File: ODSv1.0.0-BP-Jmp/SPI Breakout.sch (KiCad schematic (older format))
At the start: 3 parts, among them J12 Conn_02x10_Odd_Even, J13 Conn_02x10_Odd_Even, J14 Conn_02x10_Odd_Even

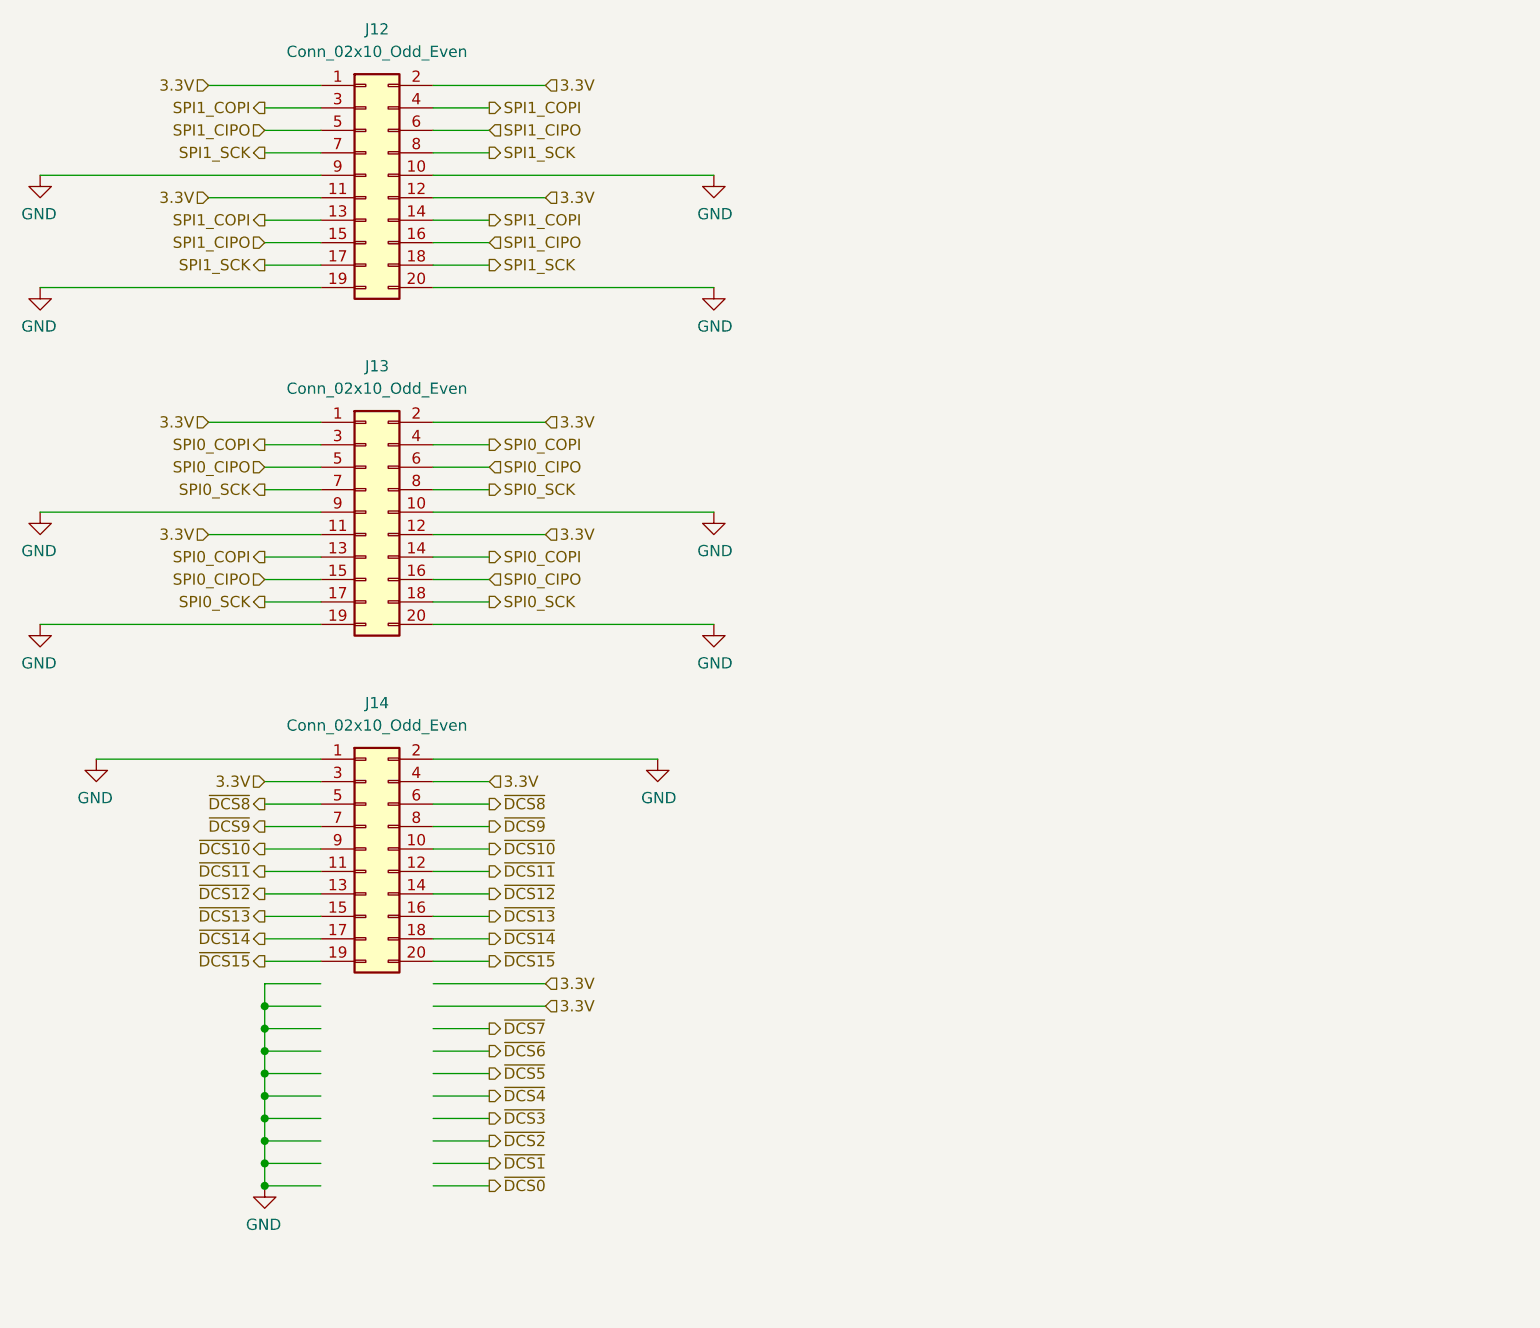
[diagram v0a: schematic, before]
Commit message: Fix hierarchical pin label directions, finish front right corner
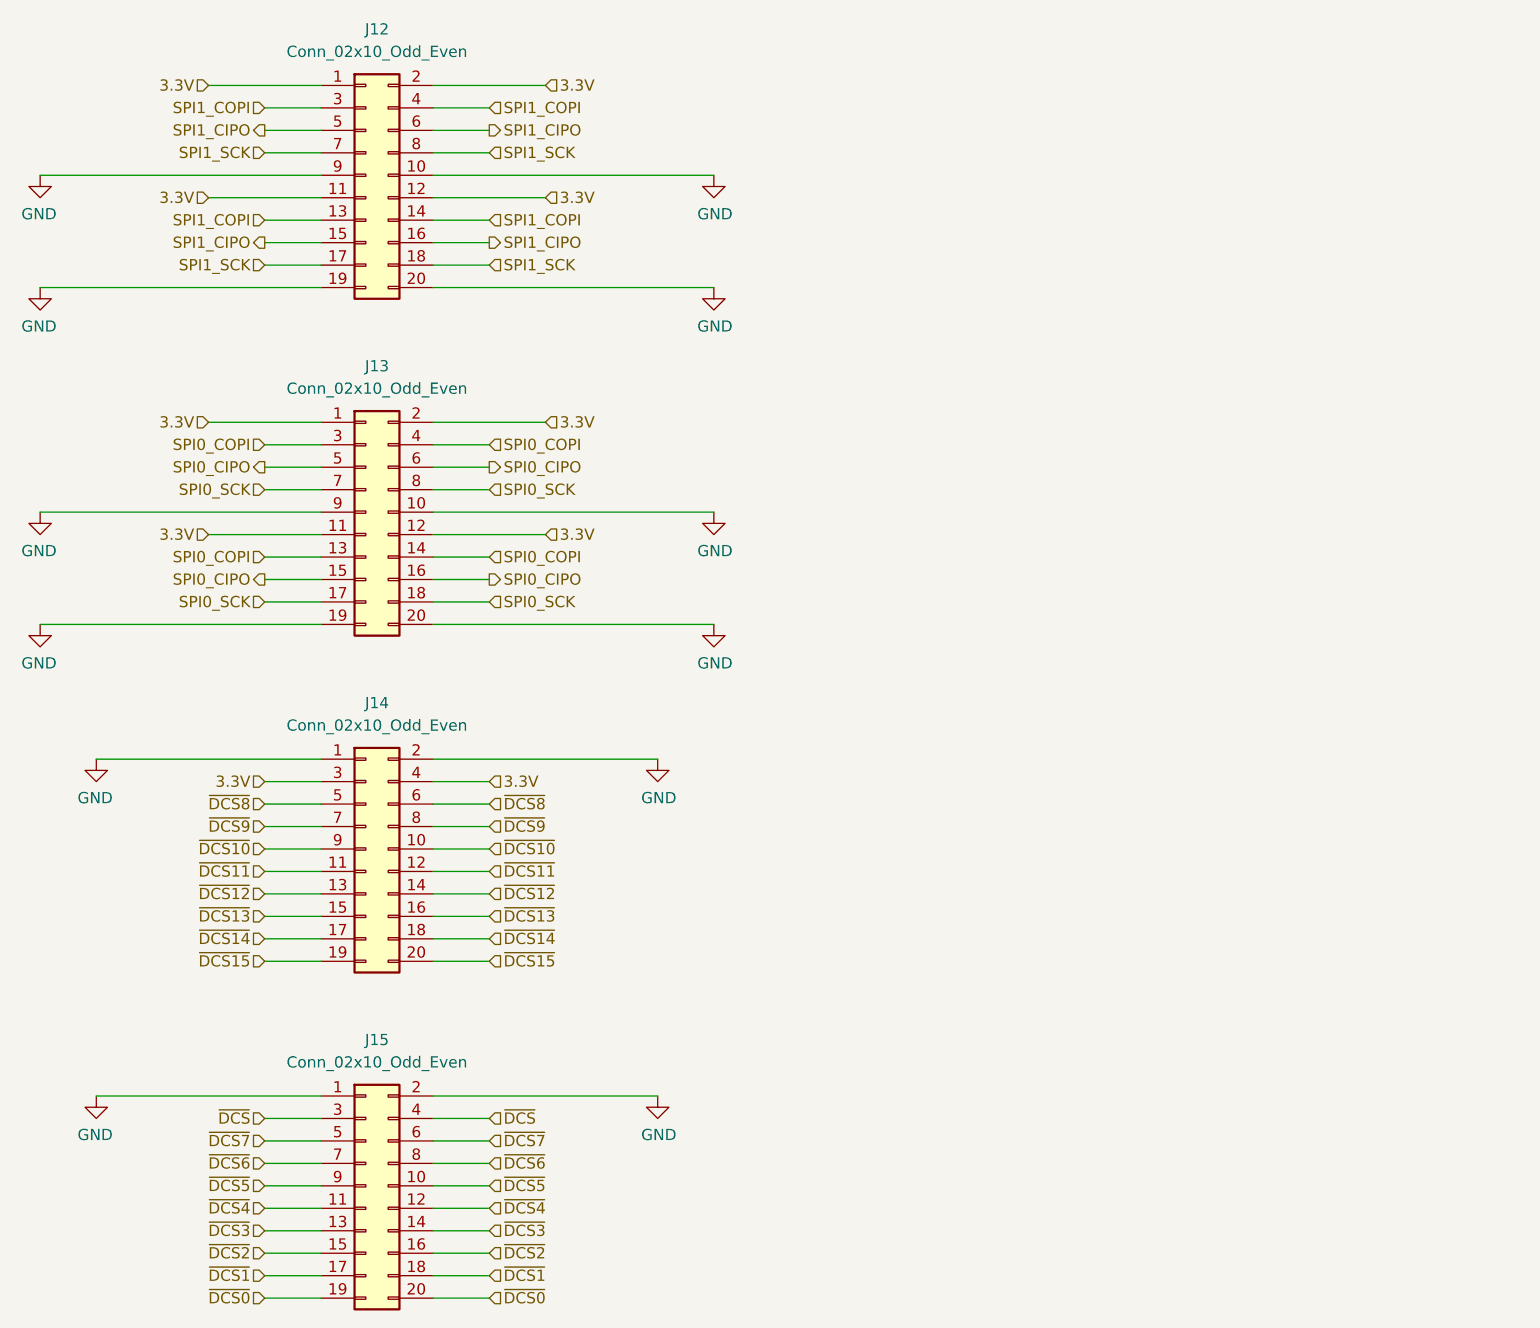
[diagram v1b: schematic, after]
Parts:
- added J15: Conn_02x10_Odd_Even, Connector_PinHeader_2.54mm:PinHeader_2x10_P2.54mm_Vertical_SMD, symbol Connector_Generic:Conn_02x10_Odd_Even
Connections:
- net labels added: ~DCS~
- wire segments 89 -> 80

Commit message: Add a DAC
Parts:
- added J18, J19: Conn_02x10_Odd_Even, Connector_PinHeader_2.54mm:PinHeader_2x10_P2.54mm_Vertical_SMD, symbol Connector_Generic:Conn_02x10_Odd_Even
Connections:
- net 3.3V: now also J18.1 (Pin_1), J18.11 (Pin_11), J18.12 (Pin_12), J18.2 (Pin_2), J19.1 (Pin_1), J19.11 (Pin_11), J19.12 (Pin_12), J19.2 (Pin_2)
- net GND: now also J18.10 (Pin_10), J18.19 (Pin_19), J18.20 (Pin_20), J18.9 (Pin_9), J19.10 (Pin_10), J19.19 (Pin_19), J19.20 (Pin_20), J19.9 (Pin_9)
- net SPI0_CIPO: now also J19.15 (Pin_15), J19.16 (Pin_16), J19.5 (Pin_5), J19.6 (Pin_6)
- net SPI0_COPI: now also J19.13 (Pin_13), J19.14 (Pin_14), J19.3 (Pin_3), J19.4 (Pin_4)
- net SPI0_SCK: now also J19.17 (Pin_17), J19.18 (Pin_18), J19.7 (Pin_7), J19.8 (Pin_8)
- net SPI1_CIPO: now also J18.15 (Pin_15), J18.16 (Pin_16), J18.5 (Pin_5), J18.6 (Pin_6)
- net SPI1_COPI: now also J18.13 (Pin_13), J18.14 (Pin_14), J18.3 (Pin_3), J18.4 (Pin_4)
- net SPI1_SCK: now also J18.17 (Pin_17), J18.18 (Pin_18), J18.7 (Pin_7), J18.8 (Pin_8)
